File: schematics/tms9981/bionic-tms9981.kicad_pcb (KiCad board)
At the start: 2 copper layers, 25.4 x 68.6 mm, 16 parts, among them J1 Bionic-P135, J2 Bionic-P245, U1 TMS9981, U2 11AA010-I/TT, U3 NJW4132

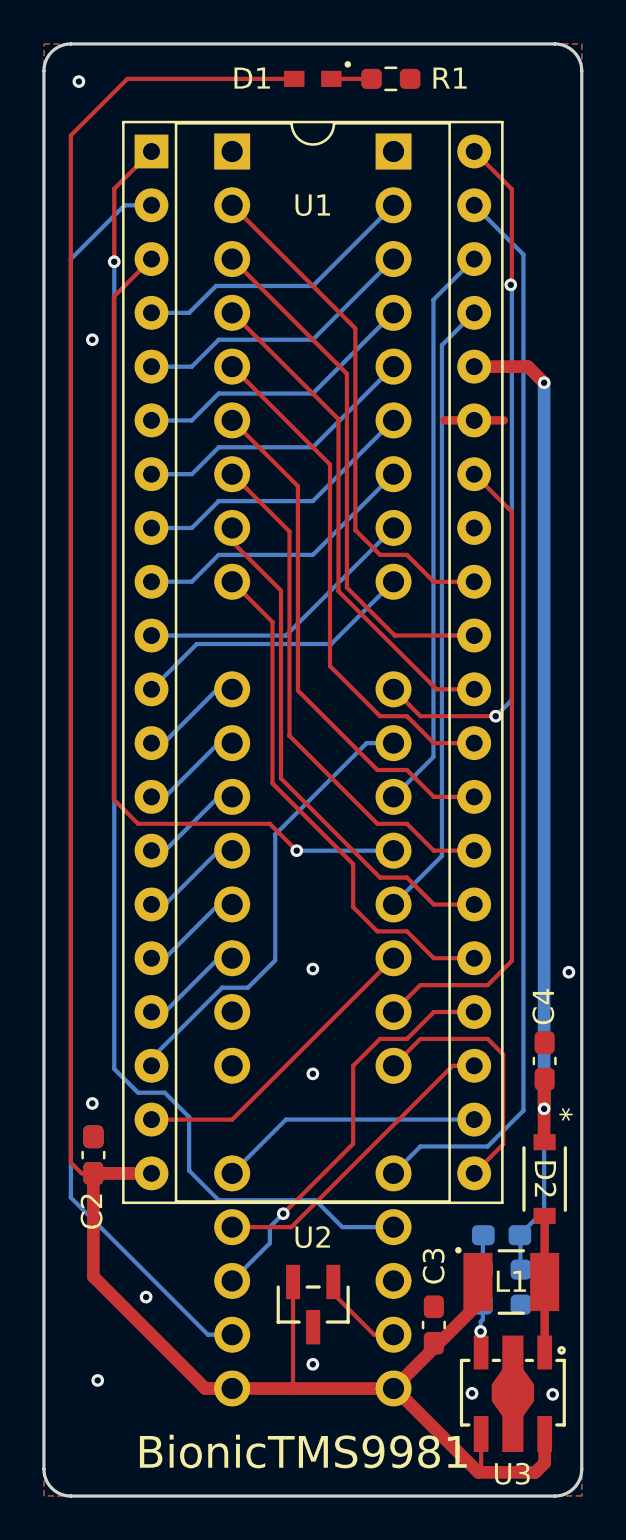
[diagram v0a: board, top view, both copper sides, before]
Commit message: [schematics] Straighten board tracks and regenerate Gerbers
straighten_tracks.py on every routed board: router leftovers snapped to
0/45/90 degrees and redundant segments merged, each pass DRC-checked
(counts unchanged). Gerbers and drill files of the changed boards are
regenerated with each board's plot settings, keeping the committed file
sets; tms9980 keeps its tracks (the rebuild left a dangling VCC stub).
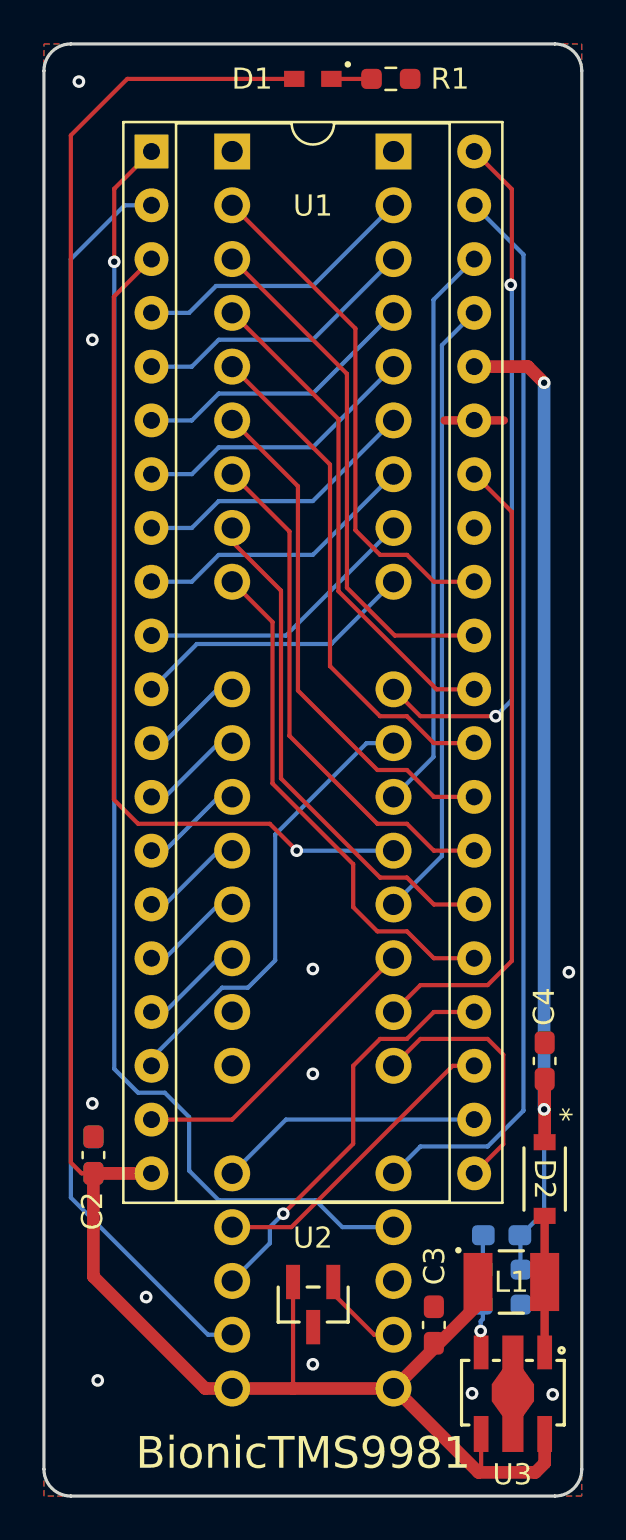
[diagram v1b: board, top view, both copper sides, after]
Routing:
- net /P35: track 4.86 -> 3.59 mm
- net /P32: track 4.86 -> 3.59 mm
- net /P34: track 4.86 -> 3.59 mm
- net /P33: track 4.86 -> 3.59 mm
- net /P31: track 4.86 -> 3.59 mm
- net /P30: track 4.86 -> 3.59 mm
- net VCC: track 112.1 -> 111.1 mm
- net /P16: track 24.4 -> 23.7 mm
- net Net-(J2-P57): track 4.20 -> 3.64 mm

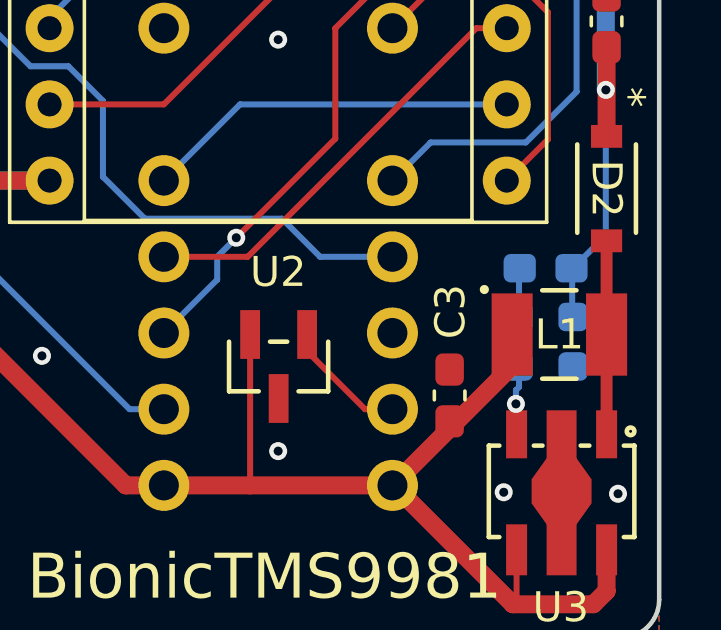
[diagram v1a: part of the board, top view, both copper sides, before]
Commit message: [schematics] Align silkscreen reference labels
align_silk.py snaps each footprint kind's labels onto their common
offset and angle and clears labels DRC flags on silkscreen; 76 labels on
22 boards, no DRC count grows. Their Gerbers are regenerated.
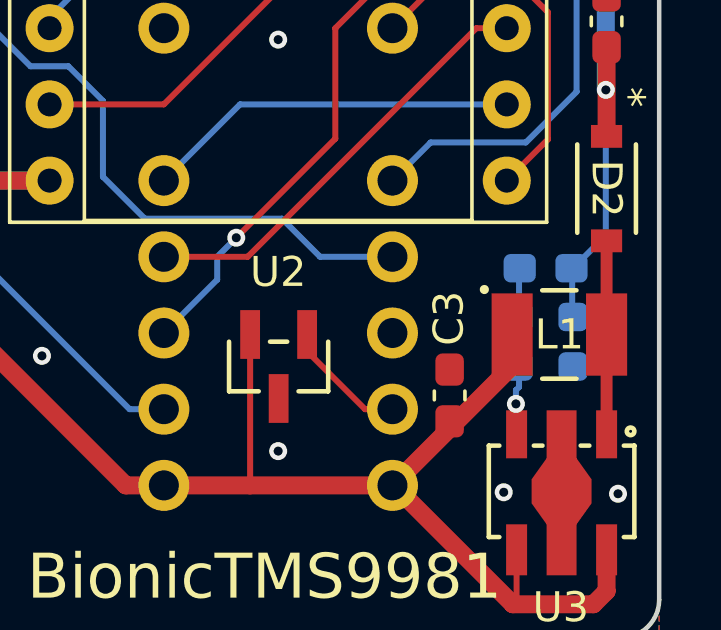
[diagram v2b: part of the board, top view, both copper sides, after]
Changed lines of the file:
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@@
 		(tags "capacitor handsolder")
 		(property "Reference" "C3"
-			(at 2.7929 0.0254 90)
+			(at 2.57 -0.03 90)
 			(layer "F.SilkS")
 			(effects

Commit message: [schematics] Remove the JLC order-number marker from all boards
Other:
- board text removed: "JLCJLCJLCJLC"
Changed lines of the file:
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@@
-		)
-	)
-	(gr_text "JLCJLCJLCJLC"
-		(at 114.208 137.056 0)
-		(layer "B.SilkS")
-		(effects
-			(font
-				(size 0.8 0.8)
-			)
-			(justify mirror)
 		)
 	)
